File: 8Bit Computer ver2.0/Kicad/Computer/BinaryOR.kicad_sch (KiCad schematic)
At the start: 4 parts, among them IC100 SN74ABT574ADWR, IC97 SN74LVC1G14DBVR, IC98 SN74AHC32DR, IC99 SN74AHC74DR

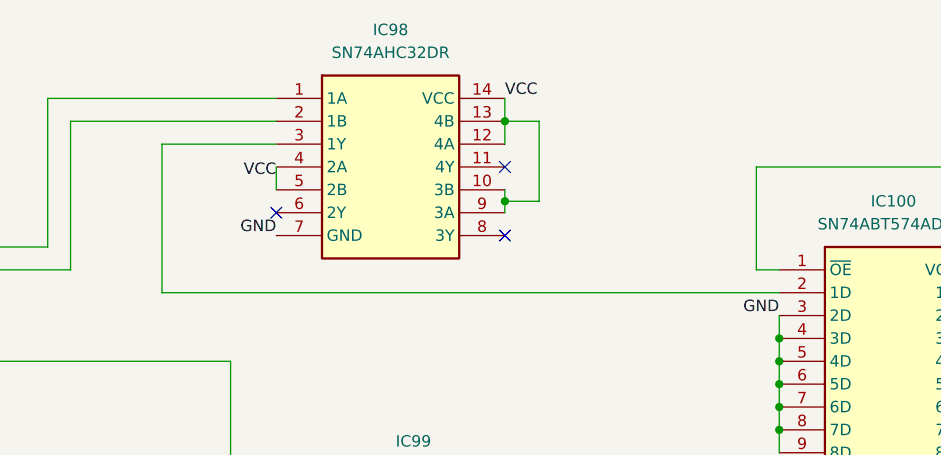
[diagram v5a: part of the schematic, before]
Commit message: Kicad
added 10pin 2,54mm Header
finished ALU PCB and added pin Header for extra use (DAT,ADR,CMD,Ddis,CLK)
31.12-06.01 about +60hr for ALU
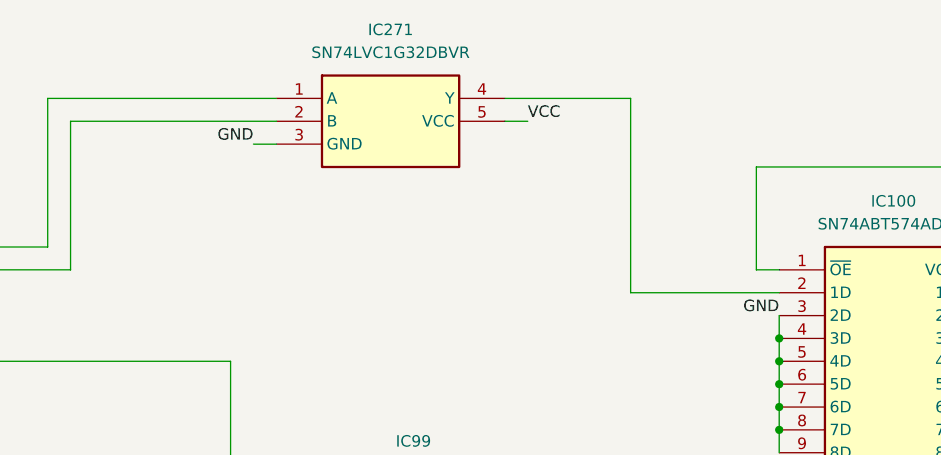
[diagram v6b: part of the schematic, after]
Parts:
- removed IC98: SN74AHC32DR, Samacsys:SOIC127P600X175-14N, symbol Samacsys:SN74AHC32DR
- added IC271: SN74LVC1G32DBVR, Samacsys:SOT95P280X145-5N, symbol Samacsys:SN74LVC1G32DBVR
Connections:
- net A: now also IC271.1 (A)
- net B: now also IC271.2 (B)
- net GND: now also IC271.3 (GND)
- net VCC: now also IC271.5 (VCC)
- net at IC100.2 (1D): now also IC271.4 (Y)
- no-connect marks 5 -> 2
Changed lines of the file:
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@@
-	)
-	(junction
-		(at 149.86 69.85)
-		(diameter 0)
-		(color 0 0 0 0)
 	)
 	(junction
@@
 	)
 	(junction
-		(at 149.86 60.96)
-		(diameter 0)
-		(color 0 0 0 0)
-	)
-	(junction
 		(at 154.94 109.22)
 		(diameter 0)
@@
 	)
 	(no_connect
-		(at 149.86 66.04)
-	)
-	(no_connect
-		(at 149.86 73.66)
-	)
-	(no_connect
-		(at 124.46 71.12)
-	)
-	(no_connect
 		(at 154.94 116.84)
 	)
@@
 	(wire
 		(pts
-			(xy 149.86 60.96) (xy 149.86 63.5)
-		)
-		(stroke
-			(width 0)
-			(type default)
-		)
-	)
-	(wire
-		(pts
 			(xy 154.94 104.14) (xy 154.94 106.68)
 		)
@@
 		)
 	)
+	(wire
+		(pts
+			(xy 149.86 58.42) (xy 163.83 58.42)
+		)
+		(stroke
+			(width 0)
+			(type default)
+		)
+	)
 	(bus
 		(pts
@@
 	(wire
 		(pts
+			(xy 149.86 60.96) (xy 152.4 60.96)
+		)
+		(stroke
+			(width 0)
+			(type default)
+		)
+	)
+	(wire
+		(pts
 			(xy 205.74 90.17) (xy 212.09 90.17)
 		)
@@
 	(wire
 		(pts
-			(xy 149.86 69.85) (xy 153.67 69.85)
+			(xy 163.83 58.42) (xy 163.83 80.01)
 		)
 		(stroke
@@
 	(wire
 		(pts
-			(xy 111.76 63.5) (xy 124.46 63.5)
-		)
-		(stroke
-			(width 0)
-			(type default)
-		)
-	)
-	(wire
-		(pts
 			(xy 113.03 114.3) (xy 113.03 125.73)
 		)
@@
 	(wire
 		(pts
-			(xy 149.86 69.85) (xy 149.86 71.12)
-		)
-		(stroke
-			(width 0)
-			(type default)
-		)
-	)
-	(wire
-		(pts
 			(xy 154.94 106.68) (xy 154.94 109.22)
 		)
@@
 	(wire
 		(pts
-			(xy 180.34 80.01) (xy 111.76 80.01)
+			(xy 180.34 80.01) (xy 163.83 80.01)
 		)
 		(stroke
@@
 	(wire
 		(pts
-			(xy 111.76 80.01) (xy 111.76 63.5)
-		)
-		(stroke
-			(width 0)
-			(type default)
-		)
-	)
-	(wire
-		(pts
 			(xy 180.34 85.09) (xy 180.34 87.63)
 		)
@@
 	(wire
 		(pts
+			(xy 121.92 63.5) (xy 124.46 63.5)
+		)
+		(stroke
+			(width 0)
+			(type default)
+		)
+	)
+	(wire
+		(pts
 			(xy 205.74 80.01) (xy 212.09 80.01)
 		)
@@
 		)
 	)
-	(wire
-		(pts
-			(xy 149.86 68.58) (xy 149.86 69.85)
-		)
-		(stroke
-			(width 0)
-			(type default)
-		)
-	)
 	(bus
 		(pts
@@
 	(wire
 		(pts
-			(xy 153.67 60.96) (xy 149.86 60.96)
-		)
-		(stroke
-			(width 0)
-			(type default)
-		)
-	)
-	(wire
-		(pts
-			(xy 153.67 69.85) (xy 153.67 60.96)
-		)
-		(stroke
-			(width 0)
-			(type default)
-		)
-	)
-	(wire
-		(pts
 			(xy 177.8 66.04) (xy 177.8 77.47)
 		)
@@
 		(pts
 			(xy 59.69 80.01) (xy 55.88 80.01)
-		)
-		(stroke
-			(width 0)
-			(type default)
-		)
-	)
-	(wire
-		(pts
-			(xy 124.46 66.04) (xy 124.46 68.58)
-		)
-		(stroke
-			(width 0)
-			(type default)
-		)
-	)
-	(wire
-		(pts
-			(xy 149.86 58.42) (xy 149.86 60.96)
 		)
 		(stroke
@@
 	)
 	(label "VCC"
-		(at 124.46 67.31 180)
-		(effects
-			(font
-				(size 1.27 1.27)
-			)
-			(justify right bottom)
-		)
-	)
-	(label "VCC"
-		(at 149.86 58.42 0)
+		(at 152.4 60.96 0)
 		(effects
 			(font
@@
 	)
 	(label "GND"
-		(at 124.46 73.66 180)
+		(at 121.92 63.5 180)
 		(effects
 			(font
@@
 	)
 	(symbol
-		(lib_id "Samacsys:SN74AHC32DR")
+		(lib_id "Samacsys:SN74LVC1G32DBVR")
 		(at 124.46 58.42 0)
 		(unit 1)
@@
 		(dnp no)
 		(fields_autoplaced yes)
-		(property "Reference" "IC98"
+		(property "Reference" "IC271"
 			(at 137.16 50.8 0)
 			(effects
@@
 			)
 		)
-		(property "Value" "SN74AHC32DR"
+		(property "Value" "SN74LVC1G32DBVR"
 			(at 137.16 53.34 0)
 			(effects
@@
 			)
 		)
-		(property "Footprint" "Samacsys:SOIC127P600X175-14N"
+		(property "Footprint" "Samacsys:SOT95P280X145-5N"
 			(at 146.05 153.34 0)
 			(effects
@@
 			)
 		)
-		(property "Datasheet" "http://www.ti.com/lit/gpn/sn74ahc32"
+		(property "Datasheet" "http://www.ti.com/lit/gpn/sn74lvc1g32"
 			(at 146.05 253.34 0)
 			(effects
@@
 			)
 		)
-		(property "Description" "Quadruple 2-Input Positive-OR Gates"
+		(property "Description" "Texas Instruments SN74LVC1G32DBVR, 2-Input OR Logic Gate, 1.65  5.5 V, 5-Pin SOT-23"
 			(at 124.46 58.42 0)
 			(effects
@@
 			)
 		)
-		(property "Height" "1.75"
+		(property "Height" "1.45"
 			(at 146.05 453.34 0)
 			(effects
@@
 			)
 		)
-		(property "Mouser Part Number" "595-SN74AHC32DR"
+		(property "Mouser Part Number" "595-SN74LVC1G32DBVR"
 			(at 146.05 553.34 0)
 			(effects
@@
 			)
 		)
-		(property "Mouser Price/Stock" "https://www.mouser.co.uk/ProductDetail/Texas-Instruments/SN74AHC32DR?qs=bvpNxolhIUP1gpgKlKyYQQ%3D%3D"
+		(property "Mouser Price/Stock" "https://www.mouser.co.uk/ProductDetail/Texas-Instruments/SN74LVC1G32DBVR?qs=3pnr37ZAbK%2F6ArGi%2FPb2Ng%3D%3D"
 			(at 146.05 653.34 0)
 			(effects
@@
 			)
 		)
-		(property "Manufacturer_Part_Number" "SN74AHC32DR"
+		(property "Manufacturer_Part_Number" "SN74LVC1G32DBVR"
 			(at 146.05 853.34 0)
 			(effects
@@
 			)
 		)
+		(pin "2"
+		)
+		(pin "3"
+		)
+		(pin "5"
+		)
+		(pin "4"
+		)
 		(pin "1"
 		)
-		(pin "2"
-		)
-		(pin "3"
-		)
-		(pin "4"
-		)
-		(pin "5"
-		)
-		(pin "6"
-		)
-		(pin "7"
-		)
-		(pin "13"
-		)
-		(pin "14"
-		)
-		(pin "9"
-		)
-		(pin "10"
-		)
-		(pin "11"
-		)
-		(pin "8"
-		)
-		(pin "12"
-		)
 		(instances
-			(project "Computer"
+			(project ""
 				(path "/1196a00e-6878-4d6d-82b7-9e052dfe7c14/c4d8b530-1c6d-45af-88d2-7dc1d4321a34/f378dbdf-df8b-4230-93b7-3ecbbffd1ccb"
-					(reference "IC98")
+					(reference "IC271")
 					(unit 1)
 				)

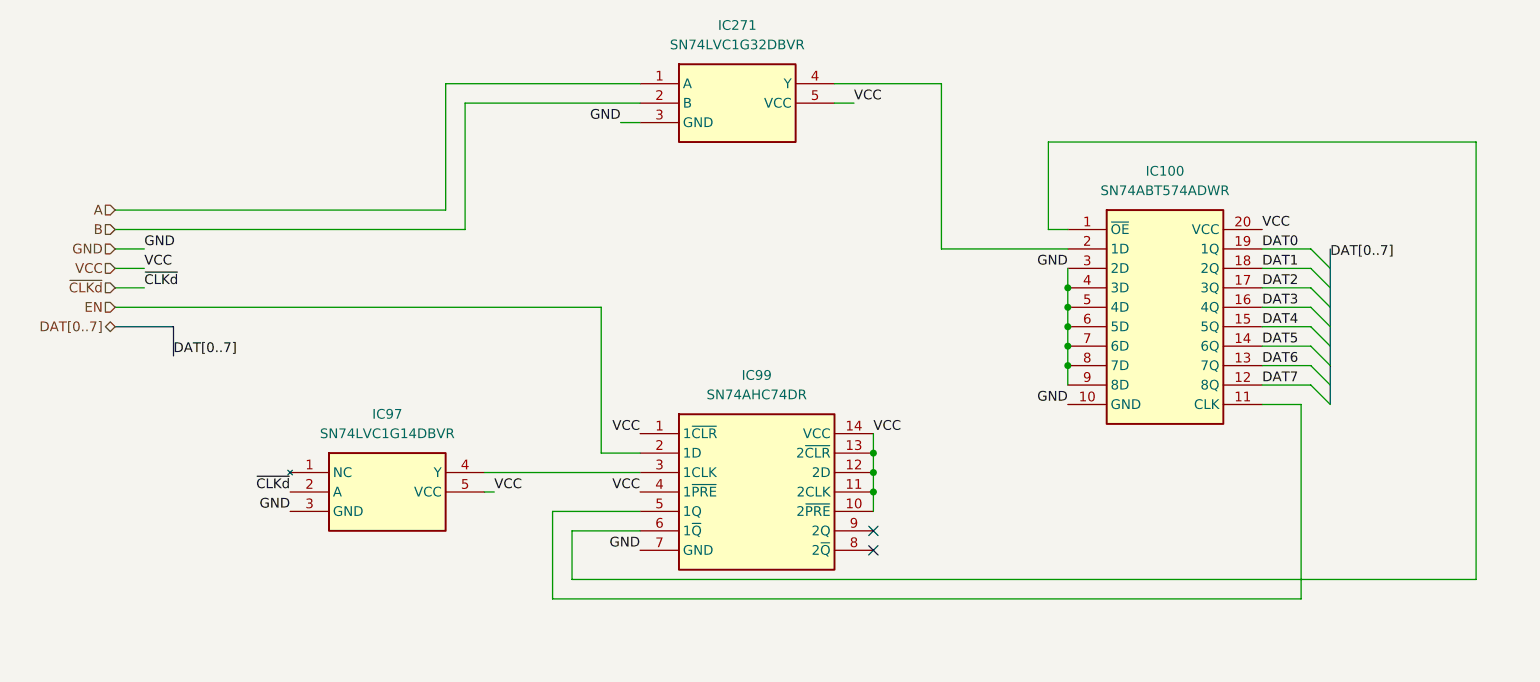
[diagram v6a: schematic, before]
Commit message: changed page numbers, compressed ROOT file from A1 to A4
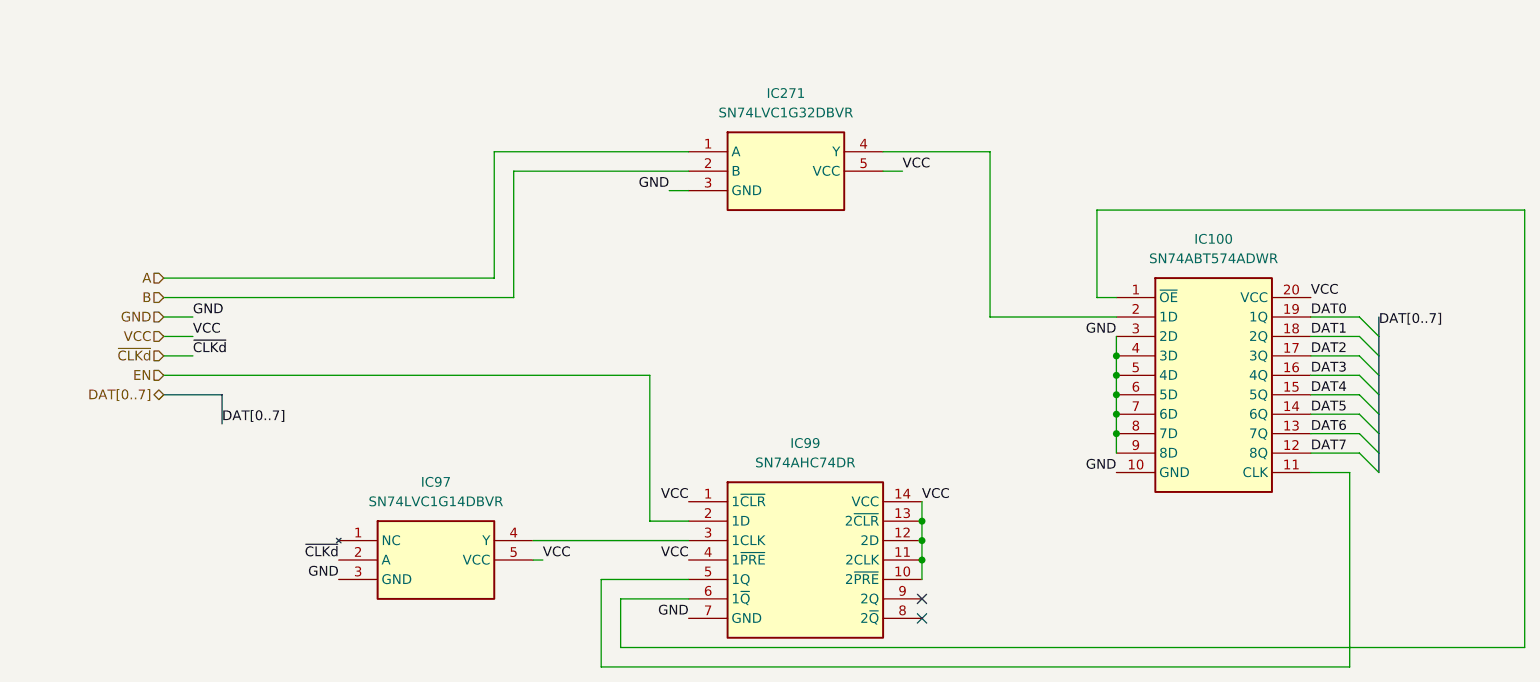
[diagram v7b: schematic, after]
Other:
- moved on the sheet: IC271

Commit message: changed page numbers, every schematic is now A4
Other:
- title: (none) -> ${SHEETNAME}
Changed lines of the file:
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@@
 	(generator_version "9.0")
 	(paper "A4")
+	(title_block
+		(title "${SHEETNAME}")
+		(date "2026-03-21")
+		(rev "2.7")
+	)
 	(junction
 		(at 161.29 115.57)
